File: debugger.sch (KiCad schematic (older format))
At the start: 14 parts, among them J2 USB_B_Micro, J5 Conn_ARM_JTAG_SWD_10, J6 Conn_ARM_JTAG_SWD_10, U7 STM32F048G6Ux

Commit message: Fix 1V8 issue and OSPI pinout
Signed-off-by: Martin Ribelotta <martinribelotta@gmail.com>
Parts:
- added C22: 1u, Capacitor_SMD:C_0603_1608Metric, symbol Device:C_Small
- added JP3: Jumper_NO_Small, Jumper:SolderJumper-2_P1.3mm_Open_TrianglePad1.0x1.5mm, symbol Device:Jumper_NO_Small
- added U11: LP38691SD-1.8, Package_SON:WSON-6-1EP_3x3mm_P0.95mm, symbol Regulator_Linear:LP38691SD-1.8
- C27: value 100n -> 1u
- J5: MANUFACTURER (none) -> CNC Tech; MANUFACTURER_PART_NUMBER (none) -> HPH2-A-10-UA-SMT
- JP2: footprint Connector_PinHeader_2.54mm:PinHeader_1x02_P2.54mm_Vertical -> Jumper:SolderJumper-2_P1.3mm_Open_RoundedPad1.0x1.5mm
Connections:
- net +3V3: now also C22.1, JP3.2, U11.1 (IN), U11.6 (IN); no longer C27.1, U7.17 (VDD)
- net GND: now also C22.2, U11.2 (GND), U11.7 (EP)
- new net: C27.1, JP3.1, U11.4 (OUT), U11.5 (SNS), U7.17 (VDD)
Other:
- note added: "Populate only\nfor f048"
- note added: "note: stm32f048x\nuses 1v8 VCC but\nthe IO is 3V3 tolerant\nthis may work (TBC)\nbut is preferred to use\nf042 series"
- note added: "short only\nfor f042"
- moved on the sheet: C27, C28
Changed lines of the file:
@@
 L Device:C_Small C?
 U 1 1 601846E2
-P 2150 5550
+P 4550 950
 AR Path="/601846E2" Ref="C?"  Part="1"
 AR Path="/60158DDC/601846E2" Ref="C27"  Part="1"
-F 0 "C27" H 2242 5596 50  0000 L CNN
-F 1 "100n" H 2242 5505 50  0000 L CNN
-F 2 "Capacitor_SMD:C_0603_1608Metric" H 2150 5550 50  0001 C CNN
-F 3 "~" H 2150 5550 50  0001 C CNN
-F 4 "Capacitor 100n 0603" H 2150 5550 50  0001 C CNN "DESCRIPTION"
-F 5 "CC0603KRX7R9BB104" H 2150 5550 50  0001 C CNN "MANUFACTURER_PART_NUMBER"
-F 6 "Yageo" H 2150 5550 50  0001 C CNN "MANUFACTURER"
-	1    2150 5550
+F 0 "C27" H 4642 996 50  0000 L CNN
+F 1 "1u" H 4642 905 50  0000 L CNN
+F 2 "Capacitor_SMD:C_0603_1608Metric" H 4550 950 50  0001 C CNN
+F 3 "~" H 4550 950 50  0001 C CNN
+F 4 "Capacitor 100n 0603" H 4550 950 50  0001 C CNN "DESCRIPTION"
+F 5 "CC0603KRX7R9BB104" H 4550 950 50  0001 C CNN "MANUFACTURER_PART_NUMBER"
+F 6 "Yageo" H 4550 950 50  0001 C CNN "MANUFACTURER"
+	1    4550 950
 	1    0    0    -1
 $EndComp
@@
 L Device:C_Small C?
 U 1 1 601846E8
-P 2500 5550
+P 6750 1550
 AR Path="/601846E8" Ref="C?"  Part="1"
 AR Path="/60158DDC/601846E8" Ref="C28"  Part="1"
-F 0 "C28" H 2592 5596 50  0000 L CNN
-F 1 "100n" H 2592 5505 50  0000 L CNN
-F 2 "Capacitor_SMD:C_0603_1608Metric" H 2500 5550 50  0001 C CNN
-F 3 "~" H 2500 5550 50  0001 C CNN
-F 4 "Capacitor 100n 0603" H 2500 5550 50  0001 C CNN "DESCRIPTION"
-F 5 "CC0603KRX7R9BB104" H 2500 5550 50  0001 C CNN "MANUFACTURER_PART_NUMBER"
-F 6 "Yageo" H 2500 5550 50  0001 C CNN "MANUFACTURER"
-	1    2500 5550
-	1    0    0    -1
-$EndComp
-Connection ~ 2150 5650
-Wire Wire Line
-	2150 5650 2500 5650
-Connection ~ 2150 5450
-Wire Wire Line
-	2500 5450 2150 5450
-$Comp
-L power:+3V3 #PWR?
-U 1 1 601846FE
-P 2150 5450
-AR Path="/601846FE" Ref="#PWR?"  Part="1"
-AR Path="/60158DDC/601846FE" Ref="#PWR035"  Part="1"
-F 0 "#PWR035" H 2150 5300 50  0001 C CNN
-F 1 "+3.3V" H 2165 5623 50  0000 C CNN
-F 2 "" H 2150 5450 50  0000 C CNN
-F 3 "" H 2150 5450 50  0000 C CNN
-	1    2150 5450
-	1    0    0    -1
+F 0 "C28" V 6979 1550 50  0000 C CNN
+F 1 "100n" V 6888 1550 50  0000 C CNN
+F 2 "Capacitor_SMD:C_0603_1608Metric" H 6750 1550 50  0001 C CNN
+F 3 "~" H 6750 1550 50  0001 C CNN
+F 4 "Capacitor 100n 0603" H 6750 1550 50  0001 C CNN "DESCRIPTION"
+F 5 "CC0603KRX7R9BB104" H 6750 1550 50  0001 C CNN "MANUFACTURER_PART_NUMBER"
+F 6 "Yageo" H 6750 1550 50  0001 C CNN "MANUFACTURER"
+	1    6750 1550
+	0    -1   -1   0
 $EndComp
 $Comp
 L power:GND #PWR?
 U 1 1 60184705
-P 2150 5650
+P 6850 1550
 AR Path="/60184705" Ref="#PWR?"  Part="1"
 AR Path="/60158DDC/60184705" Ref="#PWR036"  Part="1"
-F 0 "#PWR036" H 2150 5400 50  0001 C CNN
-F 1 "GND" H 2155 5477 50  0000 C CNN
-F 2 "" H 2150 5650 50  0000 C CNN
-F 3 "" H 2150 5650 50  0000 C CNN
-	1    2150 5650
+F 0 "#PWR036" H 6850 1300 50  0001 C CNN
+F 1 "GND" H 6855 1377 50  0000 C CNN
+F 2 "" H 6850 1550 50  0000 C CNN
+F 3 "" H 6850 1550 50  0000 C CNN
+	1    6850 1550
 	1    0    0    -1
 $EndComp
@@
 F 0 "JP2" V 1396 5648 50  0000 L CNN
 F 1 "Jumper_NO_Small" V 1305 5648 50  0000 L CNN
-F 2 "Connector_PinHeader_2.54mm:PinHeader_1x02_P2.54mm_Vertical" H 1350 5600 50  0001 C CNN
+F 2 "Jumper:SolderJumper-2_P1.3mm_Open_RoundedPad1.0x1.5mm" H 1350 5600 50  0001 C CNN
 F 3 "~" H 1350 5600 50  0001 C CNN
 	1    1350 5600
@@
 F 2 "Connector_PinHeader_1.27mm:PinHeader_2x05_P1.27mm_Vertical_SMD" H 4400 5450 50  0001 C CNN
 F 3 "http://infocenter.arm.com/help/topic/com.arm.doc.ddi0314h/DDI0314H_coresight_components_trm.pdf" V 4050 4200 50  0001 C CNN
+F 4 "CNC Tech" H 4400 5450 50  0001 C CNN "MANUFACTURER"
+F 5 "HPH2-A-10-UA-SMT" H 4400 5450 50  0001 C CNN "MANUFACTURER_PART_NUMBER"
 	1    4400 5450
 	1    0    0    -1
@@
 $EndComp
 Wire Wire Line
-	5750 1550 5850 1550
-Wire Wire Line
 	5950 1550 5950 1450
 Connection ~ 5950 1550
-Connection ~ 5850 1550
 Wire Wire Line
 	5850 1550 5950 1550
@@
 P 4900 3050
 AR Path="/608F7DDB" Ref="#PWR?"  Part="1"
-AR Path="/60158DDC/608F7DDB" Ref="#PWR?"  Part="1"
-F 0 "#PWR?" H 4900 2800 50  0001 C CNN
+AR Path="/60158DDC/608F7DDB" Ref="#PWR0118"  Part="1"
+F 0 "#PWR0118" H 4900 2800 50  0001 C CNN
 F 1 "GND" V 4905 2922 50  0000 R CNN
 F 2 "" H 4900 3050 50  0000 C CNN
@@
 	0    1    1    0
 $EndComp
+Wire Wire Line
+	5750 850  5750 1550
+Wire Wire Line
+	4550 850  5750 850
+$Comp
+L power:GND #PWR?
+U 1 1 60FF0976
+P 4550 1050
+AR Path="/60FF0976" Ref="#PWR?"  Part="1"
+AR Path="/60158DDC/60FF0976" Ref="#PWR064"  Part="1"
+F 0 "#PWR064" H 4550 800 50  0001 C CNN
+F 1 "GND" H 4555 877 50  0000 C CNN
+F 2 "" H 4550 1050 50  0000 C CNN
+F 3 "" H 4550 1050 50  0000 C CNN
+	1    4550 1050
+	1    0    0    -1
+$EndComp
+Wire Wire Line
+	3550 850  3400 850
+$Comp
+L power:+3V3 #PWR?
+U 1 1 60FF4A9A
+P 3350 850
+AR Path="/60FF4A9A" Ref="#PWR?"  Part="1"
+AR Path="/60158DDC/60FF4A9A" Ref="#PWR012"  Part="1"
+F 0 "#PWR012" H 3350 700 50  0001 C CNN
+F 1 "+3.3V" V 3365 978 50  0000 L CNN
+F 2 "" H 3350 850 50  0000 C CNN
+F 3 "" H 3350 850 50  0000 C CNN
+	1    3350 850
+	0    -1   -1   0
+$EndComp
+$Comp
+L Device:Jumper_NO_Small JP3
+U 1 1 60FF6FA9
+P 5850 850
+F 0 "JP3" H 5850 1035 50  0000 C CNN
+F 1 "Jumper_NO_Small" H 5850 944 50  0000 C CNN
+F 2 "Jumper:SolderJumper-2_P1.3mm_Open_TrianglePad1.0x1.5mm" H 5850 850 50  0001 C CNN
+F 3 "~" H 5850 850 50  0001 C CNN
+	1    5850 850
+	1    0    0    -1
+$EndComp
+Connection ~ 5750 850
+$Comp
+L power:+3V3 #PWR?
+U 1 1 60FF7565
+P 5950 850
+AR Path="/60FF7565" Ref="#PWR?"  Part="1"
+AR Path="/60158DDC/60FF7565" Ref="#PWR065"  Part="1"
+F 0 "#PWR065" H 5950 700 50  0001 C CNN
+F 1 "+3.3V" V 5965 978 50  0000 L CNN
+F 2 "" H 5950 850 50  0000 C CNN
+F 3 "" H 5950 850 50  0000 C CNN
+	1    5950 850
+	0    1    1    0
+$EndComp
+Wire Notes Line
+	2950 550  2950 1350
+Wire Notes Line
+	2950 1350 4450 1350
+Wire Notes Line
+	4450 1350 4450 550
+Wire Notes Line
+	4450 550  2950 550
+Text Notes 3500 1550 0    50   ~ 0
+Populate only\nfor f048
+Text Notes 5800 1100 0    50   ~ 0
+short only\nfor f042
+Wire Notes Line
+	6400 950  6400 600
+Wire Notes Line
+	6400 600  5500 600
+Wire Notes Line
+	5500 600  5500 950
+Wire Notes Line
+	5500 950  6400 950
+Wire Wire Line
+	5950 1550 6650 1550
+Text Notes 7350 2950 0    50   ~ 0
+note: stm32f048x\nuses 1v8 VCC but\nthe IO is 3V3 tolerant\nthis may work (TBC)\nbut is preferred to use\nf042 series
+Wire Notes Line
+	7300 2400 7300 3050
+Wire Notes Line
+	7300 3050 8300 3050
+Wire Notes Line
+	8300 3050 8300 2400
+Wire Notes Line
+	8300 2400 7300 2400
+$Comp
+L Regulator_Linear:LP38691SD-1.8 U11
+U 1 1 61068ACA
+P 3950 950
+F 0 "U11" H 3950 1292 50  0000 C CNN
+F 1 "LP38691SD-1.8" H 3950 1201 50  0000 C CNN
+F 2 "Package_SON:WSON-6-1EP_3x3mm_P0.95mm" H 3950 950 50  0001 C CNN
+F 3 "https://www.ti.com/lit/ds/symlink/lp38691.pdf" H 3950 950 50  0001 C CNN
+	1    3950 950
+	1    0    0    -1
+$EndComp
+Wire Wire Line
+	4350 950  4350 850
+Wire Wire Line
+	4350 850  4550 850
+Connection ~ 4350 850
+Connection ~ 4550 850
+Wire Wire Line
+	3950 1250 4050 1250
+Wire Wire Line
+	4350 1250 4350 1050
+Wire Wire Line
+	4350 1050 4550 1050
+Connection ~ 4050 1250
+Wire Wire Line
+	4050 1250 4350 1250
+Connection ~ 4550 1050
+$Comp
+L Device:C_Small C?
+U 1 1 6108B1C0
+P 3400 950
+AR Path="/6108B1C0" Ref="C?"  Part="1"
+AR Path="/60158DDC/6108B1C0" Ref="C22"  Part="1"
+F 0 "C22" H 3492 996 50  0000 L CNN
+F 1 "1u" H 3492 905 50  0000 L CNN
+F 2 "Capacitor_SMD:C_0603_1608Metric" H 3400 950 50  0001 C CNN
+F 3 "~" H 3400 950 50  0001 C CNN
+F 4 "Capacitor 100n 0603" H 3400 950 50  0001 C CNN "DESCRIPTION"
+F 5 "CC0603KRX7R9BB104" H 3400 950 50  0001 C CNN "MANUFACTURER_PART_NUMBER"
+F 6 "Yageo" H 3400 950 50  0001 C CNN "MANUFACTURER"
+	1    3400 950
+	1    0    0    -1
+$EndComp
+Connection ~ 3400 850
+Wire Wire Line
+	3400 850  3350 850
+Wire Wire Line
+	3950 1250 3400 1250
+Wire Wire Line
+	3400 1250 3400 1050
+Connection ~ 3950 1250
 $EndSCHEMATC

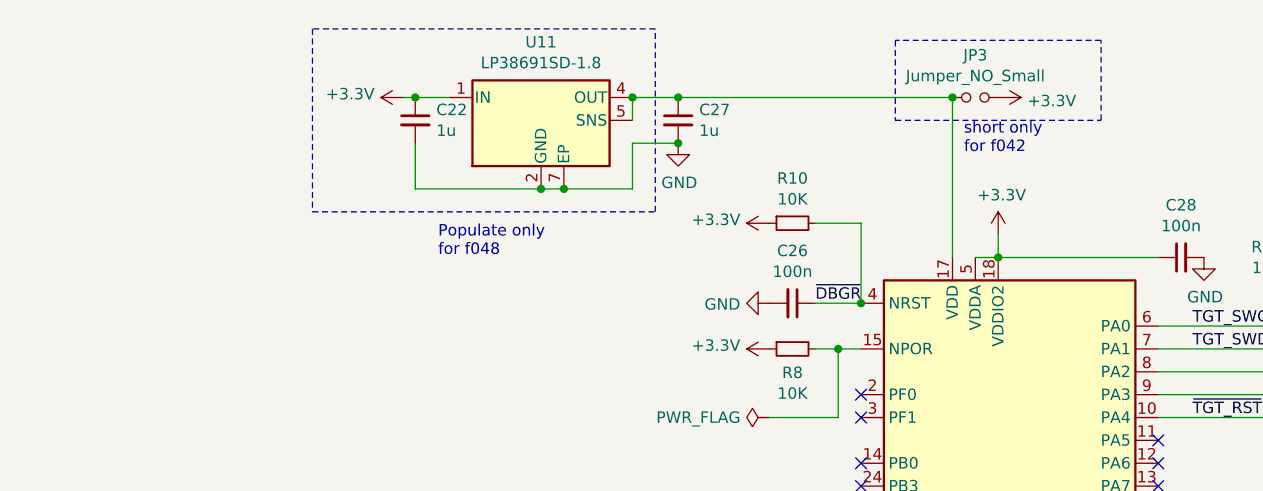
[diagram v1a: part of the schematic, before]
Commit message: Change 1V8 regulator for a more cheap and small part
Signed-off-by: Martin Ribelotta <martinribelotta@gmail.com>
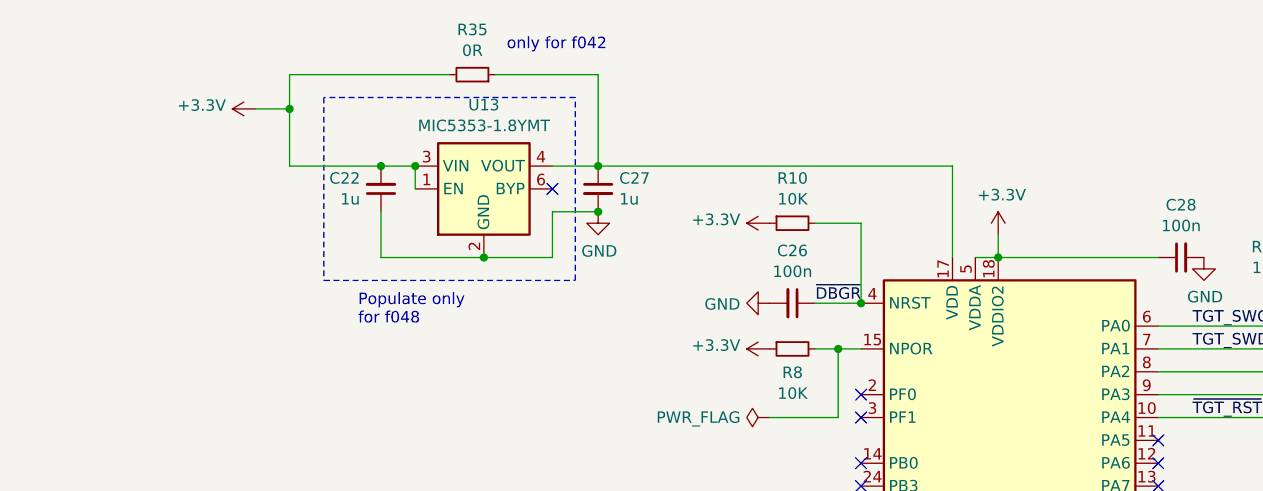
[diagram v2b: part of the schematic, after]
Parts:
- removed JP3: Jumper_NO_Small, Jumper:SolderJumper-2_P1.3mm_Open_TrianglePad1.0x1.5mm, symbol Device:Jumper_NO_Small
- removed U11: LP38691SD-1.8, Package_SON:WSON-6-1EP_3x3mm_P0.95mm, symbol Regulator_Linear:LP38691SD-1.8
- added R35: 0R, Resistor_SMD:R_0603_1608Metric, symbol Device:R_Small
- added U13: MIC5353-1.8YMT, Package_DFN_QFN:MLF-6-1EP_1.6x1.6mm_P0.5mm_EP0.5x1.26mm, symbol Regulator_Linear:MIC5353-1.8YMT
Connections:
- net +3V3: now also C22.2, R35.2, U13.1 (EN), U13.3 (VIN); no longer C22.1
- net GND: now also C22.1, U13.2 (GND), U13.7 (GND); no longer C22.2
- net at C27.1, U7.17 (VDD): now also R35.1, U13.4 (VOUT)
- no-connect marks 17 -> 18
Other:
- note added: "only for f042"
- note removed: "short only\nfor f042"
- moved on the sheet: C22, C27
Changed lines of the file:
@@
 L Device:C_Small C?
 U 1 1 601846E2
-P 4550 950
+P 4200 1250
 AR Path="/601846E2" Ref="C?"  Part="1"
 AR Path="/60158DDC/601846E2" Ref="C27"  Part="1"
-F 0 "C27" H 4642 996 50  0000 L CNN
-F 1 "1u" H 4642 905 50  0000 L CNN
-F 2 "Capacitor_SMD:C_0603_1608Metric" H 4550 950 50  0001 C CNN
-F 3 "~" H 4550 950 50  0001 C CNN
-F 4 "Capacitor 100n 0603" H 4550 950 50  0001 C CNN "DESCRIPTION"
-F 5 "CC0603KRX7R9BB104" H 4550 950 50  0001 C CNN "MANUFACTURER_PART_NUMBER"
-F 6 "Yageo" H 4550 950 50  0001 C CNN "MANUFACTURER"
-	1    4550 950
+F 0 "C27" H 4292 1296 50  0000 L CNN
+F 1 "1u" H 4292 1205 50  0000 L CNN
+F 2 "Capacitor_SMD:C_0603_1608Metric" H 4200 1250 50  0001 C CNN
+F 3 "~" H 4200 1250 50  0001 C CNN
+F 4 "Capacitor 100n 0603" H 4200 1250 50  0001 C CNN "DESCRIPTION"
+F 5 "CC0603KRX7R9BB104" H 4200 1250 50  0001 C CNN "MANUFACTURER_PART_NUMBER"
+F 6 "Yageo" H 4200 1250 50  0001 C CNN "MANUFACTURER"
+	1    4200 1250
 	1    0    0    -1
 $EndComp
@@
 $EndComp
 Wire Wire Line
-	5750 850  5750 1550
-Wire Wire Line
-	4550 850  5750 850
+	5750 1150 5750 1550
 $Comp
 L power:GND #PWR?
 U 1 1 60FF0976
-P 4550 1050
+P 4200 1350
 AR Path="/60FF0976" Ref="#PWR?"  Part="1"
 AR Path="/60158DDC/60FF0976" Ref="#PWR064"  Part="1"
-F 0 "#PWR064" H 4550 800 50  0001 C CNN
-F 1 "GND" H 4555 877 50  0000 C CNN
-F 2 "" H 4550 1050 50  0000 C CNN
-F 3 "" H 4550 1050 50  0000 C CNN
-	1    4550 1050
-	1    0    0    -1
-$EndComp
-Wire Wire Line
-	3550 850  3400 850
+F 0 "#PWR064" H 4200 1100 50  0001 C CNN
+F 1 "GND" H 4205 1177 50  0000 C CNN
+F 2 "" H 4200 1350 50  0000 C CNN
+F 3 "" H 4200 1350 50  0000 C CNN
+	1    4200 1350
+	1    0    0    -1
+$EndComp
 $Comp
 L power:+3V3 #PWR?
 U 1 1 60FF4A9A
-P 3350 850
+P 2700 900
 AR Path="/60FF4A9A" Ref="#PWR?"  Part="1"
 AR Path="/60158DDC/60FF4A9A" Ref="#PWR012"  Part="1"
-F 0 "#PWR012" H 3350 700 50  0001 C CNN
-F 1 "+3.3V" V 3365 978 50  0000 L CNN
-F 2 "" H 3350 850 50  0000 C CNN
-F 3 "" H 3350 850 50  0000 C CNN
-	1    3350 850
+F 0 "#PWR012" H 2700 750 50  0001 C CNN
+F 1 "+3.3V" V 2715 1028 50  0000 L CNN
+F 2 "" H 2700 900 50  0000 C CNN
+F 3 "" H 2700 900 50  0000 C CNN
+	1    2700 900
 	0    -1   -1   0
 $EndComp
-$Comp
-L Device:Jumper_NO_Small JP3
-U 1 1 60FF6FA9
-P 5850 850
-F 0 "JP3" H 5850 1035 50  0000 C CNN
-F 1 "Jumper_NO_Small" H 5850 944 50  0000 C CNN
-F 2 "Jumper:SolderJumper-2_P1.3mm_Open_TrianglePad1.0x1.5mm" H 5850 850 50  0001 C CNN
-F 3 "~" H 5850 850 50  0001 C CNN
-	1    5850 850
-	1    0    0    -1
-$EndComp
-Connection ~ 5750 850
-$Comp
-L power:+3V3 #PWR?
-U 1 1 60FF7565
-P 5950 850
-AR Path="/60FF7565" Ref="#PWR?"  Part="1"
-AR Path="/60158DDC/60FF7565" Ref="#PWR065"  Part="1"
-F 0 "#PWR065" H 5950 700 50  0001 C CNN
-F 1 "+3.3V" V 5965 978 50  0000 L CNN
-F 2 "" H 5950 850 50  0000 C CNN
-F 3 "" H 5950 850 50  0000 C CNN
-	1    5950 850
-	0    1    1    0
-$EndComp
-Wire Notes Line
-	2950 550  2950 1350
-Wire Notes Line
-	2950 1350 4450 1350
-Wire Notes Line
-	4450 1350 4450 550
-Wire Notes Line
-	4450 550  2950 550
-Text Notes 3500 1550 0    50   ~ 0
+Wire Notes Line
+	3000 850  3000 1650
+Wire Notes Line
+	3000 1650 4100 1650
+Wire Notes Line
+	4100 1650 4100 850
+Wire Notes Line
+	4100 850  3000 850
+Text Notes 3150 1850 0    50   ~ 0
 Populate only\nfor f048
-Text Notes 5800 1100 0    50   ~ 0
-short only\nfor f042
-Wire Notes Line
-	6400 950  6400 600
-Wire Notes Line
-	6400 600  5500 600
-Wire Notes Line
-	5500 600  5500 950
-Wire Notes Line
-	5500 950  6400 950
+Text Notes 3800 650  0    50   ~ 0
+only for f042
 Wire Wire Line
 	5950 1550 6650 1550
@@
 Wire Notes Line
 	8300 2400 7300 2400
-$Comp
-L Regulator_Linear:LP38691SD-1.8 U11
-U 1 1 61068ACA
-P 3950 950
-F 0 "U11" H 3950 1292 50  0000 C CNN
-F 1 "LP38691SD-1.8" H 3950 1201 50  0000 C CNN
-F 2 "Package_SON:WSON-6-1EP_3x3mm_P0.95mm" H 3950 950 50  0001 C CNN
-F 3 "https://www.ti.com/lit/ds/symlink/lp38691.pdf" H 3950 950 50  0001 C CNN
-	1    3950 950
-	1    0    0    -1
-$EndComp
-Wire Wire Line
-	4350 950  4350 850
-Wire Wire Line
-	4350 850  4550 850
-Connection ~ 4350 850
-Connection ~ 4550 850
-Wire Wire Line
-	3950 1250 4050 1250
-Wire Wire Line
-	4350 1250 4350 1050
-Wire Wire Line
-	4350 1050 4550 1050
-Connection ~ 4050 1250
-Wire Wire Line
-	4050 1250 4350 1250
-Connection ~ 4550 1050
+Wire Wire Line
+	4000 1150 4200 1150
+Connection ~ 4200 1150
+Wire Wire Line
+	4000 1550 4000 1350
+Wire Wire Line
+	4000 1350 4200 1350
+Connection ~ 4200 1350
 $Comp
 L Device:C_Small C?
 U 1 1 6108B1C0
-P 3400 950
+P 3250 1250
 AR Path="/6108B1C0" Ref="C?"  Part="1"
 AR Path="/60158DDC/6108B1C0" Ref="C22"  Part="1"
-F 0 "C22" H 3492 996 50  0000 L CNN
-F 1 "1u" H 3492 905 50  0000 L CNN
-F 2 "Capacitor_SMD:C_0603_1608Metric" H 3400 950 50  0001 C CNN
-F 3 "~" H 3400 950 50  0001 C CNN
-F 4 "Capacitor 100n 0603" H 3400 950 50  0001 C CNN "DESCRIPTION"
-F 5 "CC0603KRX7R9BB104" H 3400 950 50  0001 C CNN "MANUFACTURER_PART_NUMBER"
-F 6 "Yageo" H 3400 950 50  0001 C CNN "MANUFACTURER"
-	1    3400 950
-	1    0    0    -1
-$EndComp
-Connection ~ 3400 850
-Wire Wire Line
-	3400 850  3350 850
-Wire Wire Line
-	3950 1250 3400 1250
-Wire Wire Line
-	3400 1250 3400 1050
-Connection ~ 3950 1250
+F 0 "C22" H 3159 1204 50  0000 R CNN
+F 1 "1u" H 3159 1295 50  0000 R CNN
+F 2 "Capacitor_SMD:C_0603_1608Metric" H 3250 1250 50  0001 C CNN
+F 3 "~" H 3250 1250 50  0001 C CNN
+F 4 "Capacitor 100n 0603" H 3250 1250 50  0001 C CNN "DESCRIPTION"
+F 5 "CC0603KRX7R9BB104" H 3250 1250 50  0001 C CNN "MANUFACTURER_PART_NUMBER"
+F 6 "Yageo" H 3250 1250 50  0001 C CNN "MANUFACTURER"
+	1    3250 1250
+	1    0    0    1
+$EndComp
+Connection ~ 3250 1150
+Wire Wire Line
+	3250 1550 3250 1350
+$Comp
+L Regulator_Linear:MIC5353-1.8YMT U13
+U 1 1 61077DD7
+P 3700 1250
+F 0 "U13" H 3700 1617 50  0000 C CNN
+F 1 "MIC5353-1.8YMT" H 3700 1526 50  0000 C CNN
+F 2 "Package_DFN_QFN:MLF-6-1EP_1.6x1.6mm_P0.5mm_EP0.5x1.26mm" H 3850 850 50  0001 C CNN
+F 3 "http://ww1.microchip.com/downloads/en/DeviceDoc/mic5353.pdf" H 3950 1350 50  0001 C CNN
+	1    3700 1250
+	1    0    0    -1
+$EndComp
+NoConn ~ 4000 1250
+Connection ~ 3700 1550
+Wire Wire Line
+	3700 1550 4000 1550
+Wire Wire Line
+	3250 1550 3700 1550
+Wire Wire Line
+	3400 1150 3400 1250
+Wire Wire Line
+	3250 1150 3400 1150
+Connection ~ 3400 1150
+$Comp
+L Device:R_Small R?
+U 1 1 610AE929
+P 3650 750
+AR Path="/610AE929" Ref="R?"  Part="1"
+AR Path="/60158DDC/610AE929" Ref="R35"  Part="1"
+F 0 "R35" V 3846 750 50  0000 C CNN
+F 1 "0R" V 3755 750 50  0000 C CNN
+F 2 "Resistor_SMD:R_0603_1608Metric" H 3650 750 50  0001 C CNN
+F 3 "~" H 3650 750 50  0001 C CNN
+F 4 "Resistor 10K 0603" H 3650 750 50  0001 C CNN "DESCRIPTION"
+F 5 "Yageo" H 3650 750 50  0001 C CNN "MANUFACTURER"
+F 6 "RC0603FR-0710KL" H 3650 750 50  0001 C CNN "MANUFACTURER_PART_NUMBER"
+	1    3650 750
+	0    1    -1   0
+$EndComp
+Wire Wire Line
+	4200 1150 5750 1150
+Wire Wire Line
+	3750 750  4200 750
+Wire Wire Line
+	4200 750  4200 1150
+Wire Wire Line
+	3250 1150 2850 1150
+Wire Wire Line
+	2850 1150 2850 900
+Wire Wire Line
+	2850 750  3550 750
+Wire Wire Line
+	2850 900  2700 900
+Connection ~ 2850 900
+Wire Wire Line
+	2850 900  2850 750
 $EndSCHEMATC
